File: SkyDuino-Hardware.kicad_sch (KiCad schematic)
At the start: 39 parts, among them J1 PWR, J10 AUX2, J2 BT, J3 ET, J4 Drum, J5 Filter, J6 Exhaust, J7 Cooling, J8 NTC, J9 AUX1, Q1 DMN6075S, Q2 DMN6075S, U1 LV3842, U2 TCR2EF33, U3 MAX31855KASA, U4 MAX31855KASA, U5 DRV8871

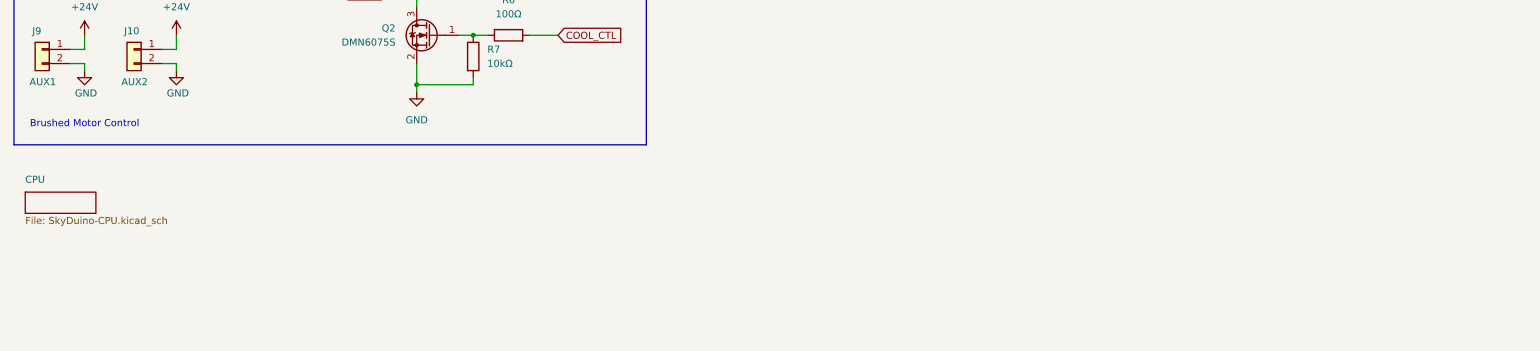
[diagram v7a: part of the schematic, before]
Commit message: Add SSR
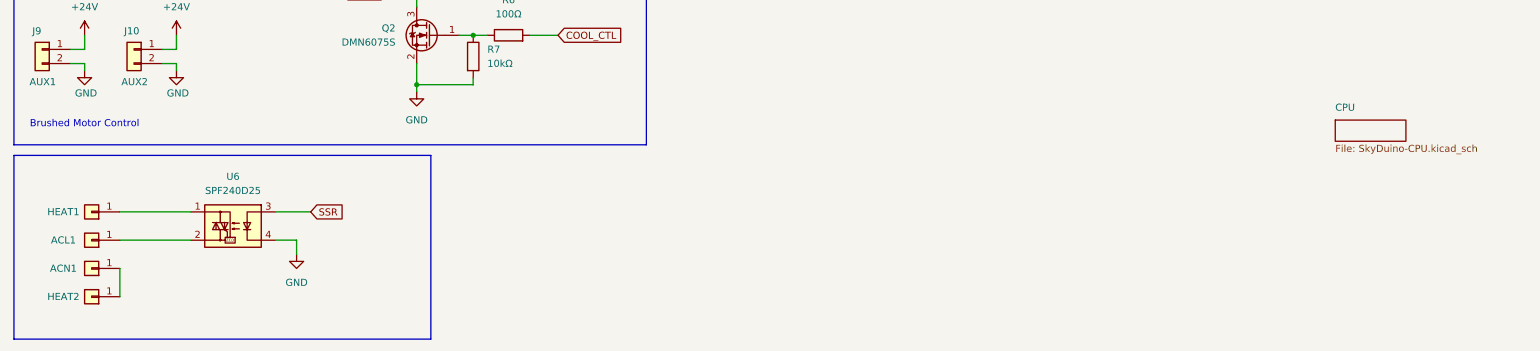
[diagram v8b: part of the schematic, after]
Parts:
- added ACL1, ACN1, HEAT1, HEAT2: Spade Conn, symbol Connector_Generic:Conn_01x01
- added U6: SPF240D25, SSRs:SSR_Crydom_SPF240D25, symbol Relay_SolidState:S102S02
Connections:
- net GND: now also U6.4
- new net: HEAT1.1 (Pin_1), U6.1
- new net: ACL1.1 (Pin_1), U6.2
- new net: ACN1.1 (Pin_1), HEAT2.1 (Pin_1)
- new net SSR: U6.3
